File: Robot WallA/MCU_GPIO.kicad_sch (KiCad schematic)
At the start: 3 parts, among them J13 10129383-916001ALF, J5 M20-8762042, J6 10129383-916001ALF

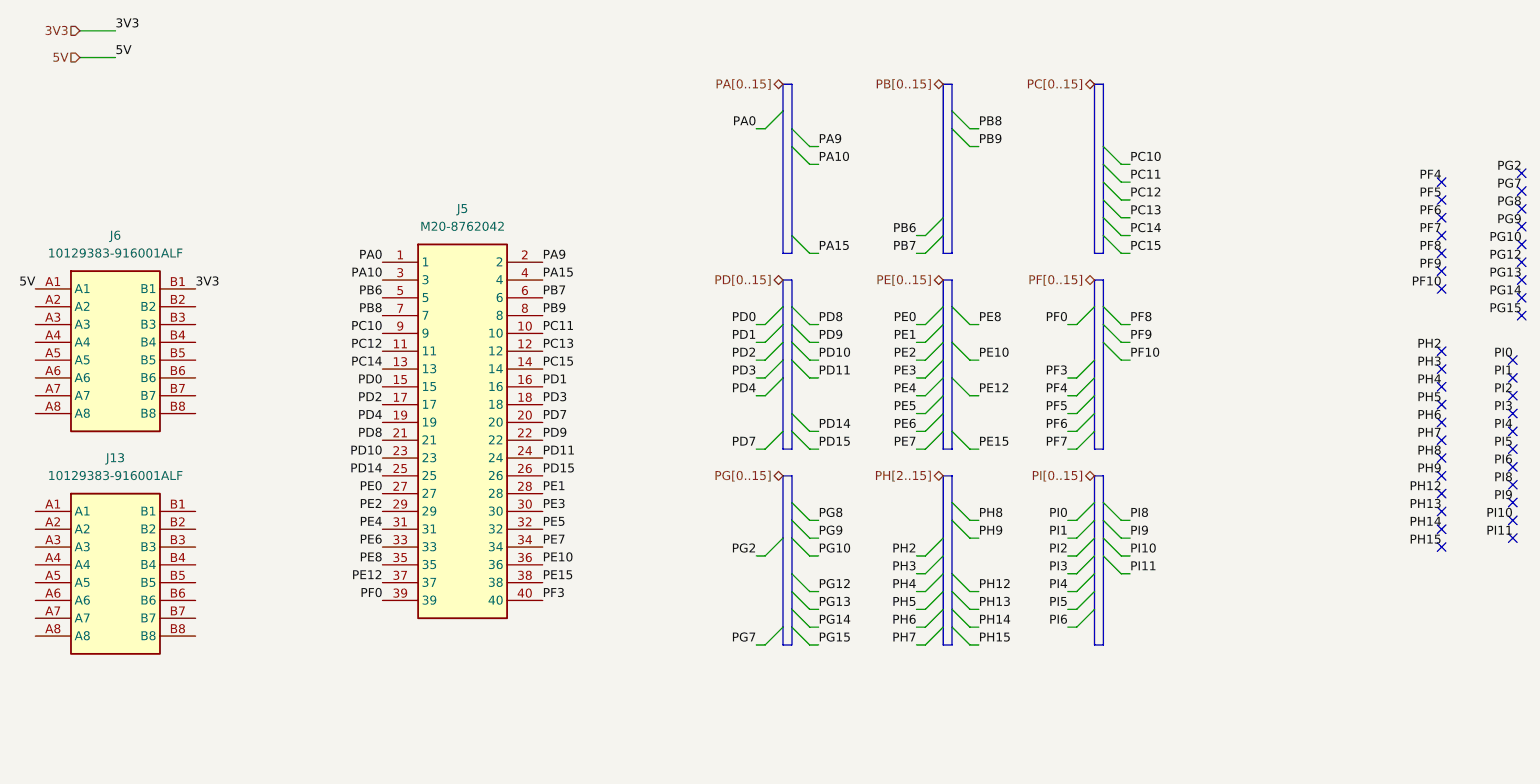
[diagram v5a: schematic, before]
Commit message: Corrected all DRC erros, added info on PCB
modified distance meter connectors to be horizontal
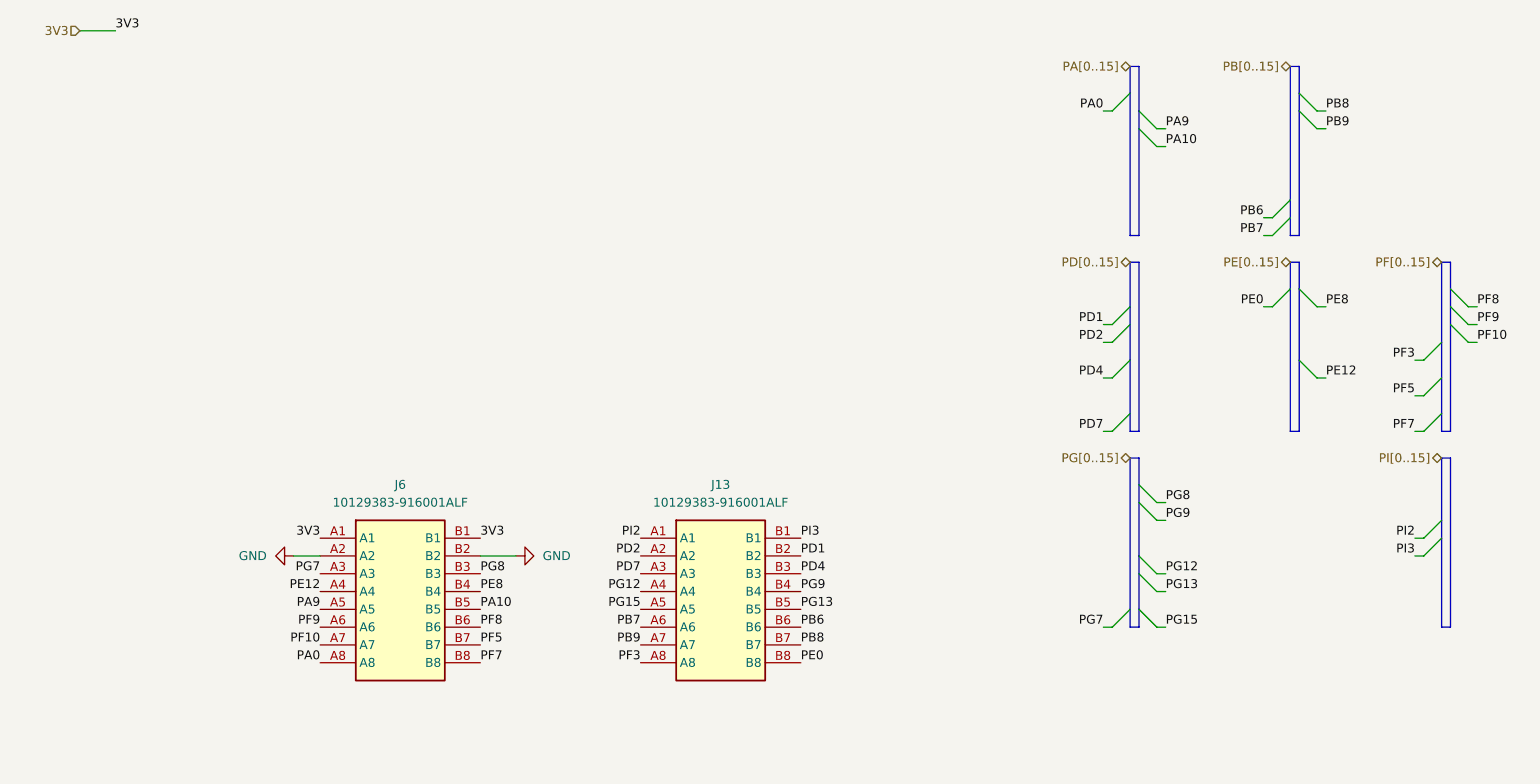
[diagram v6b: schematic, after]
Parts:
- removed J5: M20-8762042, SamacSys_Parts:M208762042, symbol SamacSys_new:M20-8762042
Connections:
- net 5V is gone; now on net 3V3: J6.A1
- net PA0: now also J6.A8
- net PA10: now also J6.B5
- net PA9: now also J6.A5
- net PB6: now also J13.B6
- net PB7: now also J13.A6
- net PB8: now also J13.B7
- net PB9: now also J13.A7
- net PD1: now also J13.B2
- net PD2: now also J13.A2
- net PD4: now also J13.B3
- net PD7: now also J13.A3
- net PE0: now also J13.B8
- net PE12: now also J6.A4
- net PE8: now also J6.B4
- net PF10: now also J6.A7
- net PF3: now also J13.A8
- net PF5: now also J6.B7
- net PF7: now also J6.B8
- net PF8: now also J6.B6
- net PF9: now also J6.A6
- net PG12: now also J13.A4
- net PG13: now also J13.B5
- net PG15: now also J13.A5
- net PG7: now also J6.A3
- net PG8: now also J6.B3
- net PG9: now also J13.B4
- net PI2: now also J13.A1
- net PI3: now also J13.B1
- net GND: now reaches J6.A2
- net GND: now also J6.B2
- no-connect marks 39 -> 0
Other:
- moved on the sheet: J13, J6

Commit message: Updated fab files.
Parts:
- J13, J6: footprint 10129383916001ALF -> SamacSys_Parts:10129383916001ALF
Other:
- company: (none) -> Socotec Monitoring
- title: (none) -> Robot Wall-A
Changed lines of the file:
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@@
 	(generator_version "9.0")
 	(paper "A4")
+	(title_block
+		(title "Robot Wall-A")
+		(date "2025-09-20")
+		(rev "v1.0")
+		(company "Socotec Monitoring")
+		(comment 1 "GDU")
+		(comment 2 "THO")
+	)
 	(bus_entry
 		(at 182.88 26.67)
@@
 			)
 		)
-		(property "Footprint" "10129383916001ALF"
+		(property "Footprint" "SamacSys_Parts:10129383916001ALF"
 			(at 132.08 185.09 0)
 			(effects
@@
 				)
 				(justify left top)
+				(hide yes)
+			)
+		)
+		(property "MPN" ""
+			(at 113.03 90.17 0)
+			(effects
+				(font
+					(size 1.27 1.27)
+				)
 				(hide yes)
 			)
@@
 			)
 		)
-		(property "Footprint" "10129383916001ALF"
+		(property "Footprint" "SamacSys_Parts:10129383916001ALF"
 			(at 86.36 185.09 0)
 			(effects
@@
 				(hide yes)
 			)
+		)
+		(property "MPN" ""
+			(at 67.31 90.17 0)
+			(effects
+				(font
+					(size 1.27 1.27)
+				)
+				(hide yes)
+			)
